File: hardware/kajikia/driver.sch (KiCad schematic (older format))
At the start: 17 parts

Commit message: reorder
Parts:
- removed C? (x4): 100n, symbol Device:C
- removed C?: 22n, symbol Device:C
- removed C? (x2): 2.2u, symbol Device:C
- removed C?: 10u, symbol Device:C
- removed C? (x2): 22u, symbol Device:C
- removed C?: 470u, symbol Device:CP1
- removed JP1, JP? (x2): SolderJumper_3_Open, symbol Jumper:SolderJumper_3_Open
- removed JP? (x2): SolderJumper_2_Open, symbol Jumper:SolderJumper_2_Open
- removed U?: TMC5160-TA, symbol _Personal:TMC5160-TA
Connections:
- net labels removed: 3.3V, 5V, CLK, CS, DCEN, DCIN, DCO, DIAG0, DIAG1, DIR, EN, GND, MISO, MOSI, OA1, OA2, OB1, OB2, SCK, STEP, Vmot
- wire segments 164 -> 0

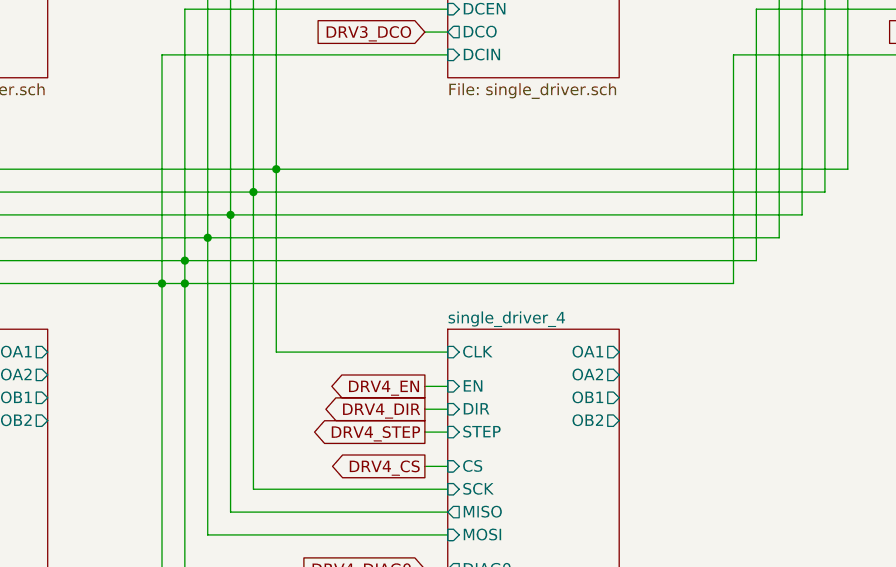
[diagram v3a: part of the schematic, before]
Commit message: switch to tmc5161
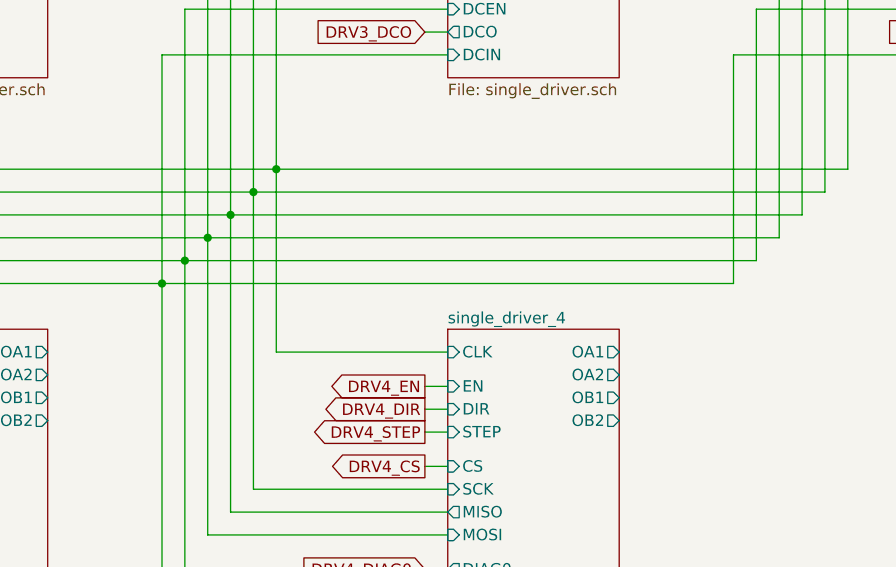
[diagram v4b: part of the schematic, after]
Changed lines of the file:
@@
 EESchema Schematic File Version 4
-LIBS:kajikia-cache
 EELAYER 26 0
 EELAYER END
 $Descr A4 11693 8268
 encoding utf-8
-Sheet 5 20
+Sheet 5 10
 Title ""
 Date ""
@@
 Wire Wire Line
 	5150 3900 7650 3900
-Wire Wire Line
-	5150 4000 7550 4000
 Connection ~ 5050 4000
 Wire Wire Line
 	5050 4000 5050 5700
 Wire Wire Line
-	5050 4000 5150 4000
-Wire Wire Line
 	5150 3900 5150 4000
-Connection ~ 5150 4000
 Wire Wire Line
 	5150 4000 5150 5500
+Wire Wire Line
+	5050 4000 7550 4000
 $EndSCHEMATC

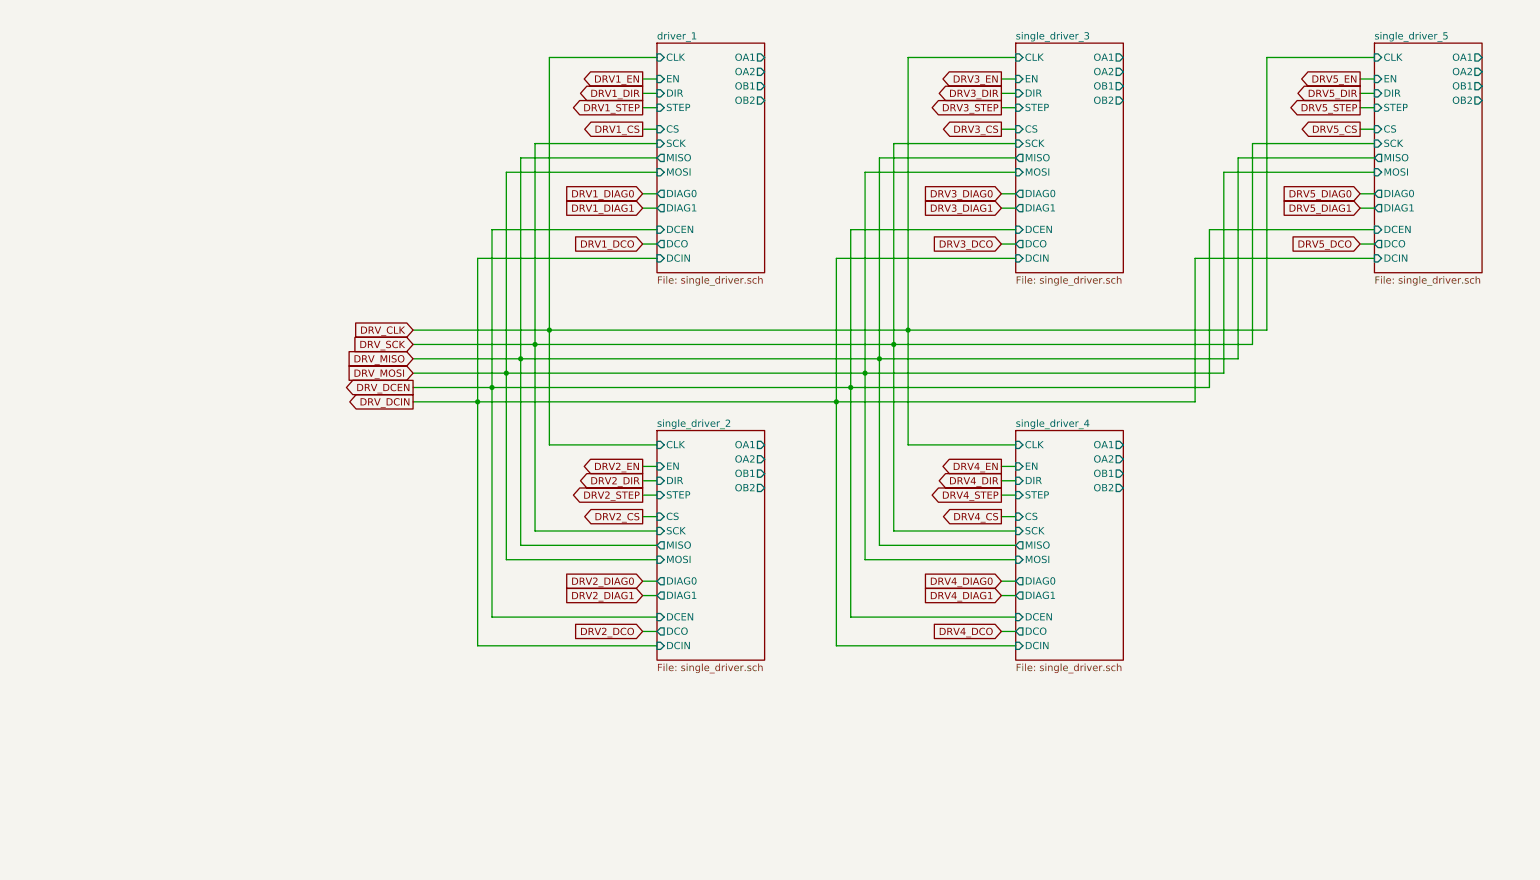
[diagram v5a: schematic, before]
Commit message: max6675, cleanup
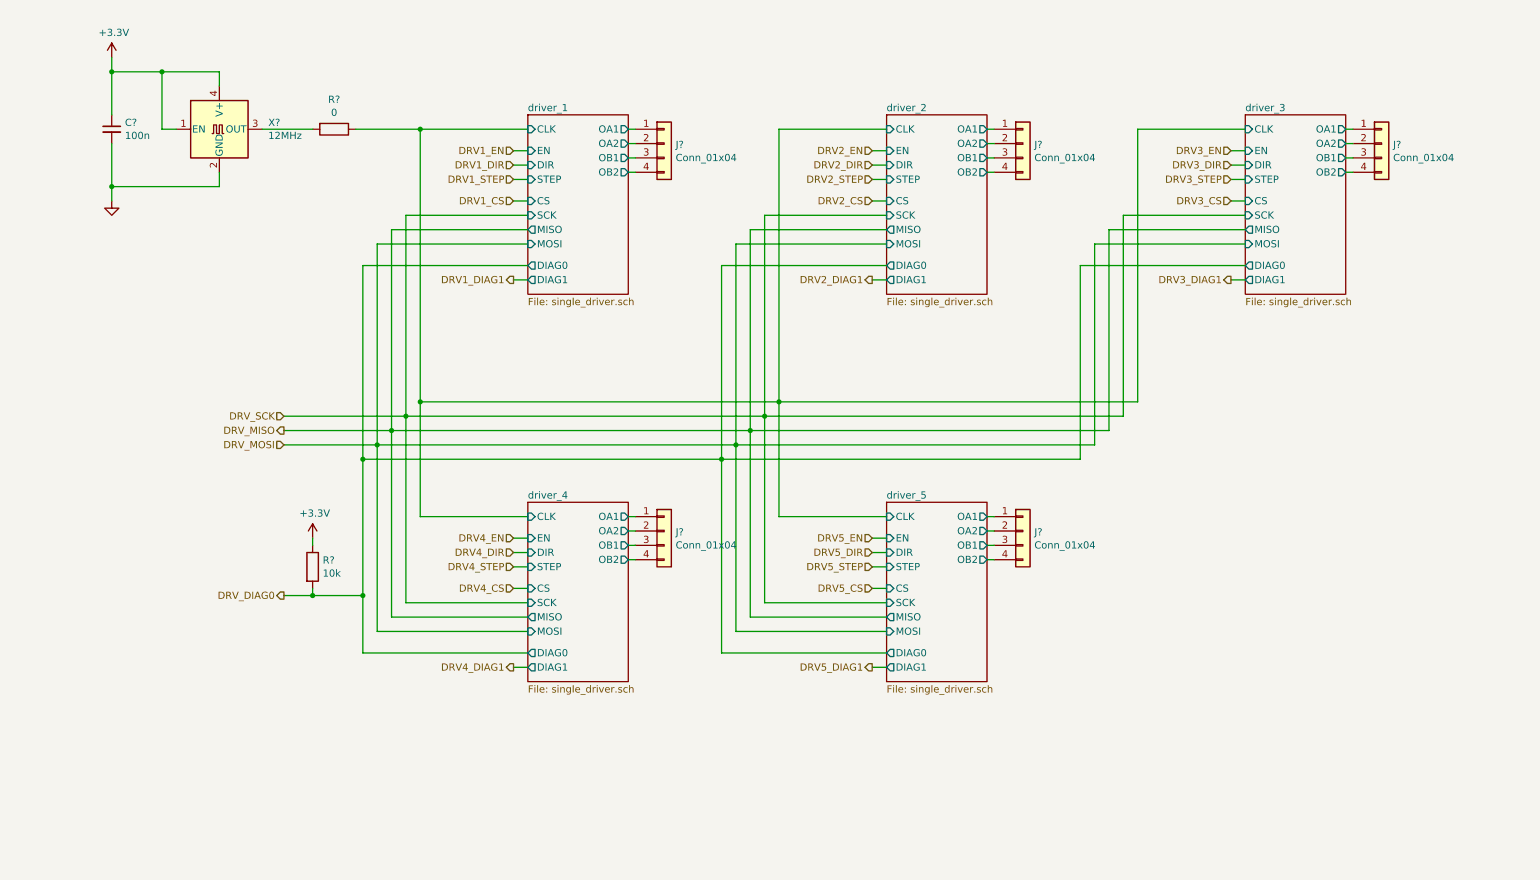
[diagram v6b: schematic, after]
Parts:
- added C?: 100n, symbol Device:C_Small
- added J? (x5): Conn_01x04, symbol Connector_Generic:Conn_01x04
- added R?: 10k, symbol Device:R
- added R?: 0, symbol Device:R
- added X?: 12MHz, Oscillator:Oscillator_SMD_EuroQuartz_XO32-4Pin_3.2x2.5mm, symbol Oscillator:XO32
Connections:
- net driver_1/OA1: now also J?.1 (Pin_1)
- net driver_1/OA2: now also J?.2 (Pin_2)
- net driver_1/OB1: now also J?.3 (Pin_3)
- net driver_1/OB2: now also J?.4 (Pin_4)
- new net: R?.2, X?.3 (OUT)
- new net +3V3: C?.1, R?.1, X?.1 (EN), X?.4 (V+)
- new net DRV_DIAG0: R?.2
- new net GND: C?.2, X?.2 (GND)
- new net driver_1/CLK: R?.1
- new net driver_2/OA1: J?.1 (Pin_1)
- new net driver_2/OA2: J?.2 (Pin_2)
- new net driver_2/OB1: J?.3 (Pin_3)
- new net driver_2/OB2: J?.4 (Pin_4)
- new net driver_3/OA1: J?.1 (Pin_1)
- new net driver_3/OA2: J?.2 (Pin_2)
- new net driver_3/OB1: J?.3 (Pin_3)
- new net driver_3/OB2: J?.4 (Pin_4)
- new net driver_4/OA1: J?.1 (Pin_1)
- new net driver_4/OA2: J?.2 (Pin_2)
- new net driver_4/OB1: J?.3 (Pin_3)
- new net driver_4/OB2: J?.4 (Pin_4)
- new net driver_5/OA1: J?.1 (Pin_1)
- new net driver_5/OA2: J?.2 (Pin_2)
- new net driver_5/OB1: J?.3 (Pin_3)
- new net driver_5/OB2: J?.4 (Pin_4)

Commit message: power
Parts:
- gave numbers to parts that had none: 9
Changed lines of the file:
@@
 F10 "DIAG0" O L 4150 2350 50
 F11 "DIAG1" O L 4150 2450 50
-F15 "OA1" O R 4850 1400 50
-F16 "OA2" O R 4850 1500 50
-F17 "OB1" O R 4850 1600 50
-F18 "OB2" O R 4850 1700 50
+F12 "OA1" O R 4850 1400 50
+F13 "OA2" O R 4850 1500 50
+F14 "OB1" O R 4850 1600 50
+F15 "OB2" O R 4850 1700 50
 $EndSheet
 Wire Wire Line
@@
 	3000 2350 4150 2350
 $Comp
-L Connector_Generic:Conn_01x04 J?
+L Connector_Generic:Conn_01x04 J68
 U 1 1 60EA0743
 P 5100 1500
-F 0 "J?" H 5180 1492 50  0000 L CNN
+AR Path="/5AF7E834/60C2EDFB/60EA0743" Ref="J68"  Part="1"
+AR Path="/5B406A82/60EA0743" Ref="J77"  Part="1"
+F 0 "J68" H 5180 1492 50  0000 L CNN
 F 1 "Conn_01x04" H 5180 1401 50  0000 L CNN
 F 2 "" H 5100 1500 50  0001 C CNN
@@
 F10 "DIAG0" O L 6650 2350 50
 F11 "DIAG1" O L 6650 2450 50
-F15 "OA1" O R 7350 1400 50
-F16 "OA2" O R 7350 1500 50
-F17 "OB1" O R 7350 1600 50
-F18 "OB2" O R 7350 1700 50
+F12 "OA1" O R 7350 1400 50
+F13 "OA2" O R 7350 1500 50
+F14 "OB1" O R 7350 1600 50
+F15 "OB2" O R 7350 1700 50
 $EndSheet
 Wire Wire Line
@@
 	5500 2350 6650 2350
 $Comp
-L Connector_Generic:Conn_01x04 J?
+L Connector_Generic:Conn_01x04 J70
 U 1 1 60ECA914
 P 7600 1500
-F 0 "J?" H 7680 1492 50  0000 L CNN
+AR Path="/5AF7E834/60C2EDFB/60ECA914" Ref="J70"  Part="1"
+AR Path="/5B406A82/60ECA914" Ref="J79"  Part="1"
+F 0 "J70" H 7680 1492 50  0000 L CNN
 F 1 "Conn_01x04" H 7680 1401 50  0000 L CNN
 F 2 "" H 7600 1500 50  0001 C CNN
@@
 F10 "DIAG0" O L 9150 2350 50
 F11 "DIAG1" O L 9150 2450 50
-F15 "OA1" O R 9850 1400 50
-F16 "OA2" O R 9850 1500 50
-F17 "OB1" O R 9850 1600 50
-F18 "OB2" O R 9850 1700 50
+F12 "OA1" O R 9850 1400 50
+F13 "OA2" O R 9850 1500 50
+F14 "OB1" O R 9850 1600 50
+F15 "OB2" O R 9850 1700 50
 $EndSheet
 Wire Wire Line
@@
 	8000 2350 9150 2350
 $Comp
-L Connector_Generic:Conn_01x04 J?
+L Connector_Generic:Conn_01x04 J72
 U 1 1 60ECD6EE
 P 10100 1500
-F 0 "J?" H 10180 1492 50  0000 L CNN
+AR Path="/5AF7E834/60C2EDFB/60ECD6EE" Ref="J72"  Part="1"
+AR Path="/5B406A82/60ECD6EE" Ref="J81"  Part="1"
+F 0 "J72" H 10180 1492 50  0000 L CNN
 F 1 "Conn_01x04" H 10180 1401 50  0000 L CNN
 F 2 "" H 10100 1500 50  0001 C CNN
@@
 F10 "DIAG0" O L 4150 5050 50
 F11 "DIAG1" O L 4150 5150 50
-F15 "OA1" O R 4850 4100 50
-F16 "OA2" O R 4850 4200 50
-F17 "OB1" O R 4850 4300 50
-F18 "OB2" O R 4850 4400 50
+F12 "OA1" O R 4850 4100 50
+F13 "OA2" O R 4850 4200 50
+F14 "OB1" O R 4850 4300 50
+F15 "OB2" O R 4850 4400 50
 $EndSheet
 Wire Wire Line
@@
 	3000 5050 4150 5050
 $Comp
-L Connector_Generic:Conn_01x04 J?
+L Connector_Generic:Conn_01x04 J69
 U 1 1 60ED5884
 P 5100 4200
-F 0 "J?" H 5180 4192 50  0000 L CNN
+AR Path="/5AF7E834/60C2EDFB/60ED5884" Ref="J69"  Part="1"
+AR Path="/5B406A82/60ED5884" Ref="J78"  Part="1"
+F 0 "J69" H 5180 4192 50  0000 L CNN
 F 1 "Conn_01x04" H 5180 4101 50  0000 L CNN
 F 2 "" H 5100 4200 50  0001 C CNN
@@
 F10 "DIAG0" O L 6650 5050 50
 F11 "DIAG1" O L 6650 5150 50
-F15 "OA1" O R 7350 4100 50
-F16 "OA2" O R 7350 4200 50
-F17 "OB1" O R 7350 4300 50
-F18 "OB2" O R 7350 4400 50
+F12 "OA1" O R 7350 4100 50
+F13 "OA2" O R 7350 4200 50
+F14 "OB1" O R 7350 4300 50
+F15 "OB2" O R 7350 4400 50
 $EndSheet
 Wire Wire Line
@@
 	5500 5050 6650 5050
 $Comp
-L Connector_Generic:Conn_01x04 J?
+L Connector_Generic:Conn_01x04 J71
 U 1 1 60ED8656
 P 7600 4200
-F 0 "J?" H 7680 4192 50  0000 L CNN
+AR Path="/5AF7E834/60C2EDFB/60ED8656" Ref="J71"  Part="1"
+AR Path="/5B406A82/60ED8656" Ref="J80"  Part="1"
+F 0 "J71" H 7680 4192 50  0000 L CNN
 F 1 "Conn_01x04" H 7680 4101 50  0000 L CNN
 F 2 "" H 7600 4200 50  0001 C CNN
@@
 	2450 4650 2650 4650
 $Comp
-L power:+3.3V #PWR?
+L power:+3.3V #PWR0188
 U 1 1 60EF0E90
 P 2650 4250
-F 0 "#PWR?" H 2650 4100 50  0001 C CNN
+AR Path="/5AF7E834/60C2EDFB/60EF0E90" Ref="#PWR0188"  Part="1"
+AR Path="/5B406A82/60EF0E90" Ref="#PWR0274"  Part="1"
+F 0 "#PWR0188" H 2650 4100 50  0001 C CNN
 F 1 "+3.3V" H 2665 4423 50  0000 C CNN
 F 2 "" H 2650 4250 50  0001 C CNN
@@
 $EndComp
 $Comp
-L Device:R R?
+L Device:R R74
 U 1 1 60EF0ED6
 P 2650 4450
-F 0 "R?" H 2720 4496 50  0000 L CNN
+AR Path="/5AF7E834/60C2EDFB/60EF0ED6" Ref="R74"  Part="1"
+AR Path="/5B406A82/60EF0ED6" Ref="R134"  Part="1"
+F 0 "R74" H 2720 4496 50  0000 L CNN
 F 1 "10k" H 2720 4405 50  0000 L CNN
 F 2 "" V 2580 4450 50  0001 C CNN
@@
 	3000 2350 3000 3700
 $Comp
-L Oscillator:XO32 X?
+L Oscillator:XO32 X1
 U 1 1 60F01ECC
 P 2000 1400
-F 0 "X?" H 2341 1446 50  0000 L CNN
+AR Path="/5AF7E834/60C2EDFB/60F01ECC" Ref="X1"  Part="1"
+AR Path="/5B406A82/60F01ECC" Ref="X2"  Part="1"
+F 0 "X1" H 2341 1446 50  0000 L CNN
 F 1 "12MHz" H 2341 1355 50  0000 L CNN
 F 2 "Oscillator:Oscillator_SMD_EuroQuartz_XO32-4Pin_3.2x2.5mm" H 2700 1050 50  0001 C CNN
@@
 $EndComp
 $Comp
-L Device:C_Small C?
+L Device:C_Small C57
 U 1 1 60F01F7D
 P 1250 1400
-F 0 "C?" H 1342 1446 50  0000 L CNN
+AR Path="/5AF7E834/60C2EDFB/60F01F7D" Ref="C57"  Part="1"
+AR Path="/5B406A82/60F01F7D" Ref="C180"  Part="1"
+F 0 "C57" H 1342 1446 50  0000 L CNN
 F 1 "100n" H 1342 1355 50  0000 L CNN
 F 2 "" H 1250 1400 50  0001 C CNN
@@
 	2000 1800 2000 1700
 $Comp
-L #Power:GND #PWR?
+L #Power:GND #PWR0189
 U 1 1 60F105B7
 P 1250 1900
-F 0 "#PWR?" H 1250 1650 50  0001 C CNN
+AR Path="/5AF7E834/60C2EDFB/60F105B7" Ref="#PWR0189"  Part="1"
+AR Path="/5B406A82/60F105B7" Ref="#PWR0275"  Part="1"
+F 0 "#PWR0189" H 1250 1650 50  0001 C CNN
 F 1 "GND" H 1250 1750 50  0001 C CNN
 F 2 "" H 1250 1900 50  0001 C CNN
@@
 Connection ~ 1250 1800
 $Comp
-L power:+3.3V #PWR?
+L power:+3.3V #PWR0190
 U 1 1 60F1567A
 P 1250 900
-F 0 "#PWR?" H 1250 750 50  0001 C CNN
+AR Path="/5AF7E834/60C2EDFB/60F1567A" Ref="#PWR0190"  Part="1"
+AR Path="/5B406A82/60F1567A" Ref="#PWR0276"  Part="1"
+F 0 "#PWR0190" H 1250 750 50  0001 C CNN
 F 1 "+3.3V" H 1265 1073 50  0000 C CNN
 F 2 "" H 1250 900 50  0001 C CNN
@@
 Connection ~ 3400 1400
 $Comp
-L Device:R R?
+L Device:R R75
 U 1 1 60F38F1C
 P 2800 1400
-F 0 "R?" V 2593 1400 50  0000 C CNN
+AR Path="/5AF7E834/60C2EDFB/60F38F1C" Ref="R75"  Part="1"
+AR Path="/5B406A82/60F38F1C" Ref="R135"  Part="1"
+F 0 "R75" V 2593 1400 50  0000 C CNN
 F 1 "0" V 2684 1400 50  0000 C CNN
 F 2 "" V 2730 1400 50  0001 C CNN

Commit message: fancy
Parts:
- C53: renamed from C57; footprint (none) -> _Generic:0603_CAP
- R66: renamed from R74; footprint (none) -> _Generic:0603_RES
- R67: renamed from R75; value 0 -> 0R; footprint (none) -> _Generic:0603_RES
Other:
- note added: "Stepper Driver Connection"
- moved on the sheet: C53, J68, J69, J70, J71, J72, R66, R67, X1
